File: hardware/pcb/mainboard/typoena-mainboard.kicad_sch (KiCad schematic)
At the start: 30 parts, among them J1 DESPI-C579, J2 UART-PROG, J3 MT3608-IN, J4 MT3608-OUT-5V, J5 BTN-JST-XH, J6 HARNESS-PCB2, Q1 AO3401A, Q2 AO3401A, Q3 2N7002, SW1 RESET, SW2 BOOT, U1 ESP32-S3-WROOM-1-N16R8, U2 AMS1117-3.3

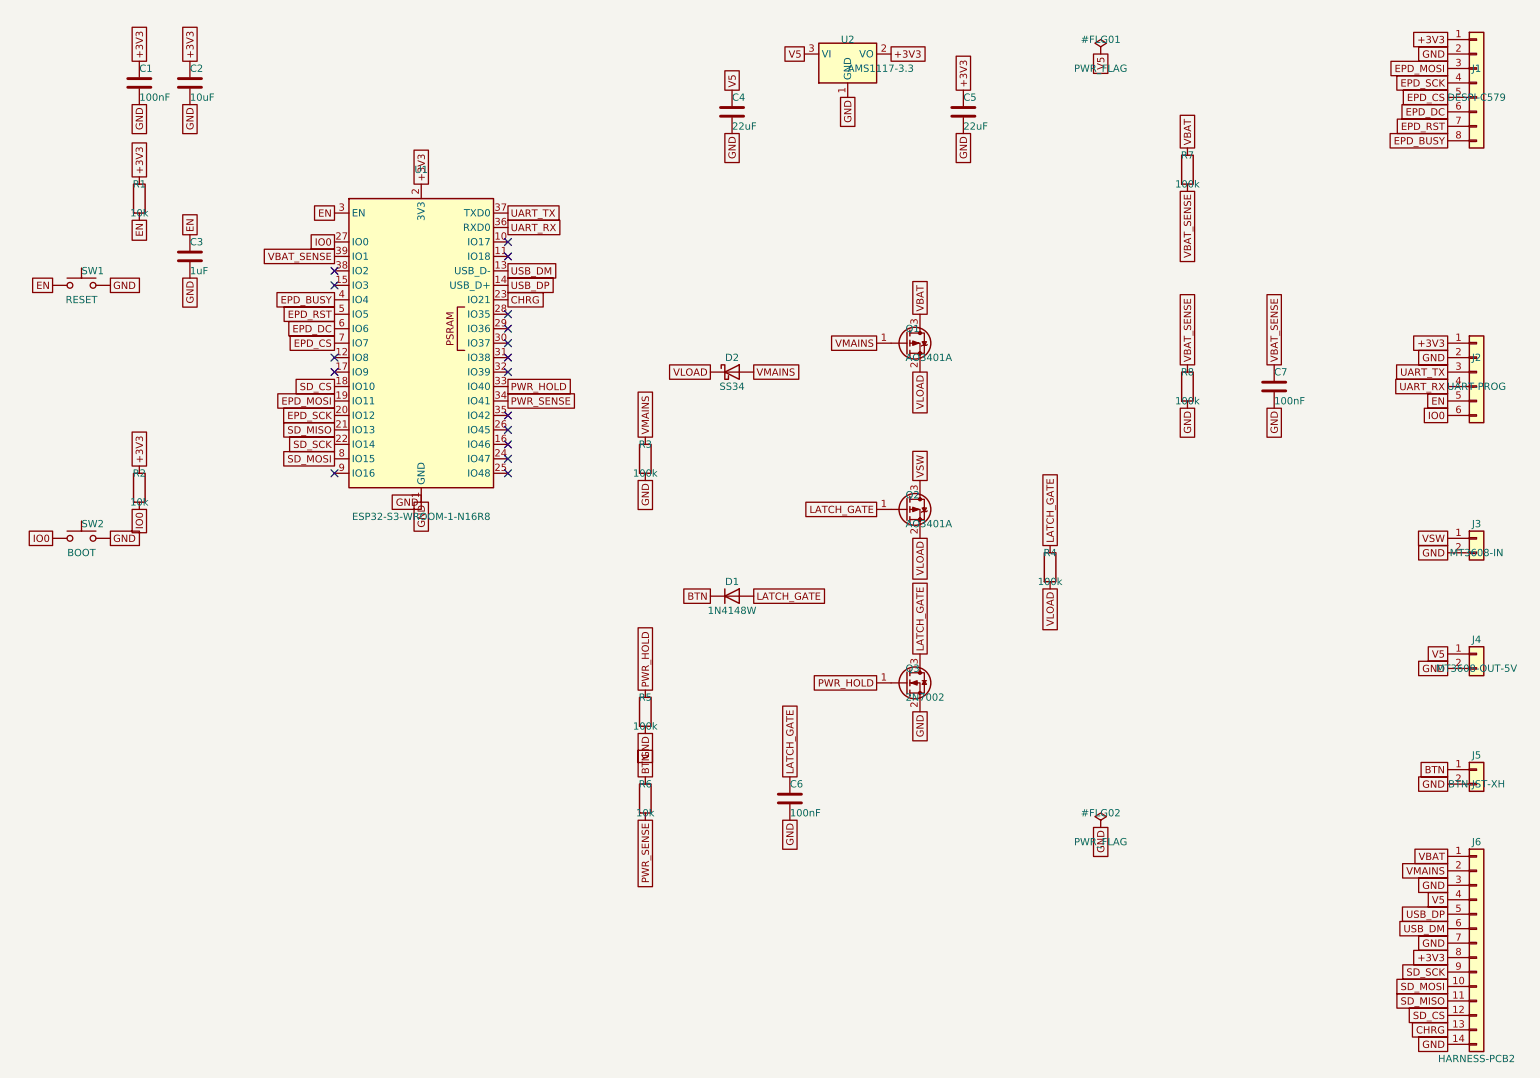
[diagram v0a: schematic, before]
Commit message: refactor(pcb): collapse to a single mainboard project
The two-perfboard design around the DevKitC-1 is gone; mainboard-v2 takes
the mainboard/ name and the -v2 suffix leaves every filename. The KiCad
project name is rewritten inside the instance blocks of all five sheets
too, otherwise KiCad drops the footprint assignments on open. ERC and DRC
still report 0 violations.

Add a Ground net class, split off Power, so GND carries its own via size
for the stitching and shows up in its own colour while routing. Its 0.2 mm
clearance is the neutral value: clearance resolves to the larger of the two
classes, so it never widens a gap on its own.

Drop the GPIO table from hardware/pcb/README.md rather than move it — the
netlist disagrees with it. PWR_HOLD no longer exists, PWR_SENSE is IO21 and
not IO41, and battery level comes from the BQ25896 over I2C instead of an
ADC. mainboard/README.md carries the pin plan that ships. wiring.md keeps
its bench-build pinout but stops attributing it to the deleted board.

hardware/bom.md, hardware/wiring.md and hardware/case/ still describe the
bench build, tracked as a TODO in the mainboard README.

Co-Authored-By: Claude Opus 5 <noreply@anthropic.com>
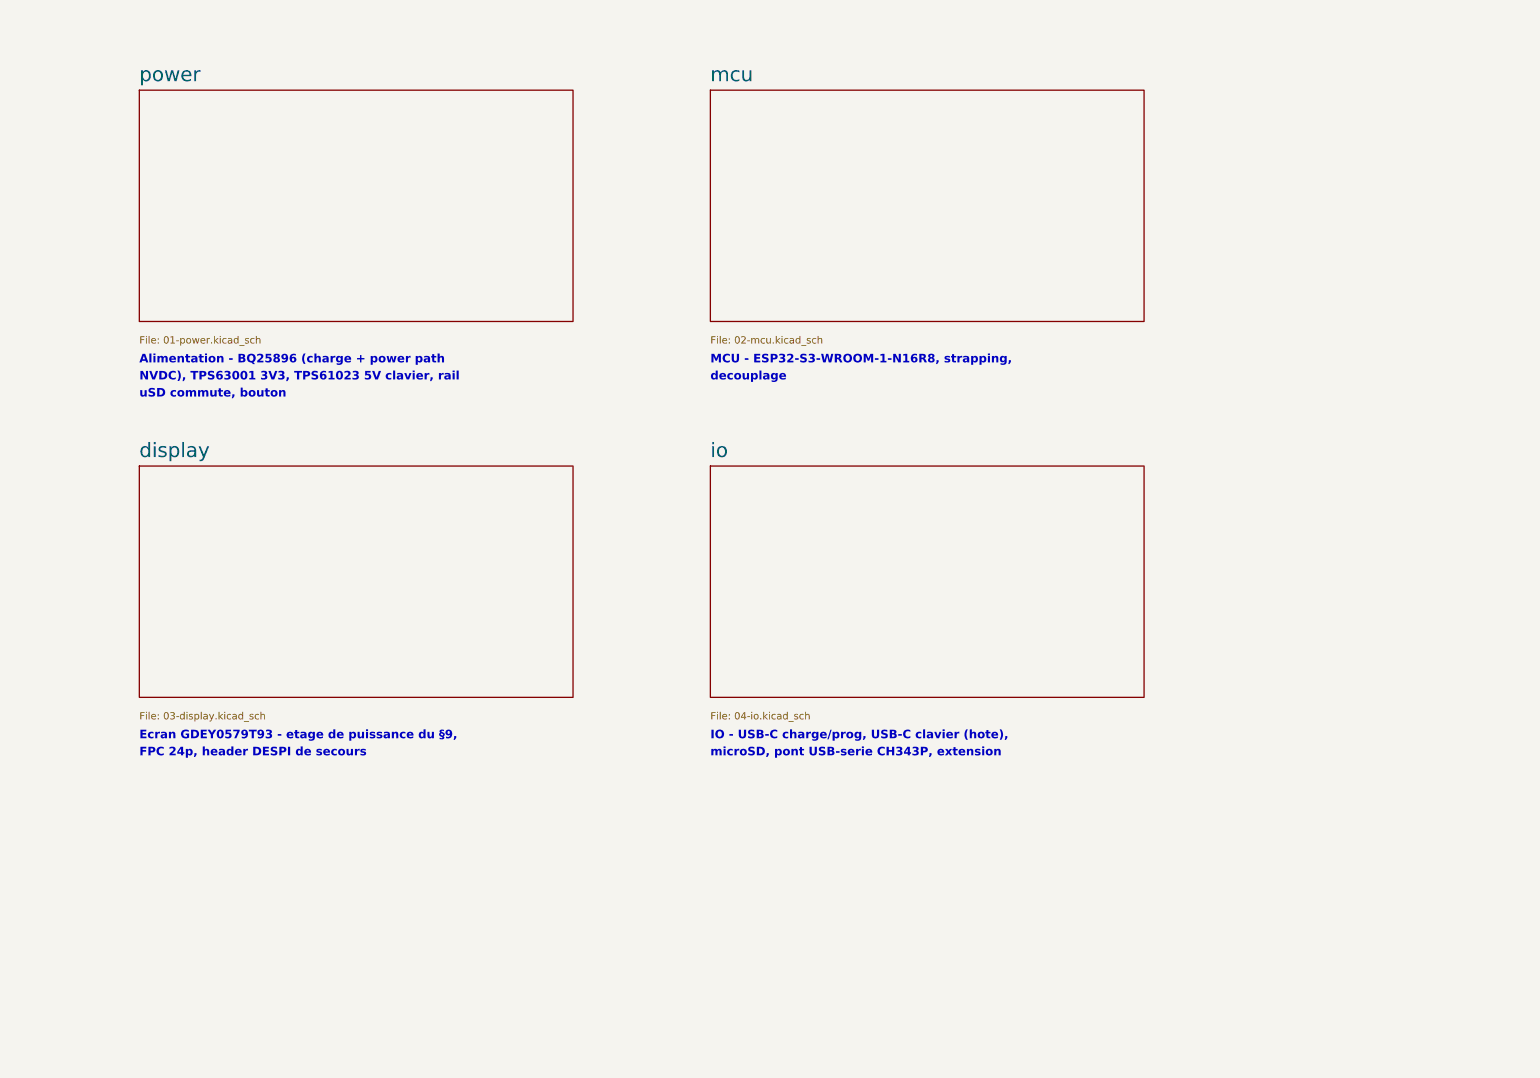
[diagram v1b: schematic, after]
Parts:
- removed C1, C6, C7: 100nF, Capacitor_SMD:C_0805_2012Metric, symbol Device:C
- removed C2: 10uF, Capacitor_SMD:C_0805_2012Metric, symbol Device:C
- removed C3: 1uF, Capacitor_SMD:C_0805_2012Metric, symbol Device:C
- removed C4, C5: 22uF, Capacitor_SMD:C_0805_2012Metric, symbol Device:C
- removed D1: 1N4148W, Diode_SMD:D_SOD-123, symbol Diode:1N4148W
- removed D2: SS34, Diode_SMD:D_SMA, symbol Diode:SS34
- removed J1: DESPI-C579, Connector_PinHeader_2.54mm:PinHeader_1x08_P2.54mm_Vertical, symbol Connector_Generic:Conn_01x08
- removed J2: UART-PROG, Connector_PinHeader_2.54mm:PinHeader_1x06_P2.54mm_Vertical, symbol Connector_Generic:Conn_01x06
- removed J3: MT3608-IN, Connector_PinHeader_2.54mm:PinHeader_1x02_P2.54mm_Vertical, symbol Connector_Generic:Conn_01x02
- removed J4: MT3608-OUT-5V, Connector_PinHeader_2.54mm:PinHeader_1x02_P2.54mm_Vertical, symbol Connector_Generic:Conn_01x02
- removed J5: BTN-JST-XH, Connector_PinHeader_2.54mm:PinHeader_1x02_P2.54mm_Vertical, symbol Connector_Generic:Conn_01x02
- removed J6: HARNESS-PCB2, Connector_PinHeader_2.54mm:PinHeader_1x14_P2.54mm_Vertical, symbol Connector_Generic:Conn_01x14
- removed Q1, Q2: AO3401A, Package_TO_SOT_SMD:SOT-23, symbol Transistor_FET:AO3401A
- removed Q3: 2N7002, Package_TO_SOT_SMD:SOT-23, symbol Transistor_FET:2N7002
- removed R1, R2, R6: 10k, Resistor_SMD:R_0805_2012Metric, symbol Device:R
- removed R3, R4, R5, R7, R8: 100k, Resistor_SMD:R_0805_2012Metric, symbol Device:R
- removed SW1: RESET, Button_Switch_SMD:SW_SPST_B3U-1000P, symbol Switch:SW_Push
- removed SW2: BOOT, Button_Switch_SMD:SW_SPST_B3U-1000P, symbol Switch:SW_Push
- removed U1: ESP32-S3-WROOM-1-N16R8, RF_Module:ESP32-S3-WROOM-1, symbol RF_Module:ESP32-S3-WROOM-1
- removed U2: AMS1117-3.3, Package_TO_SOT_SMD:SOT-223-3_TabPin2, symbol Regulator_Linear:AMS1117-3.3
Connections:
- no-connect marks 17 -> 0
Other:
- added sheet display (03-display.kicad_sch)
- added sheet io (04-io.kicad_sch)
- added sheet mcu (02-mcu.kicad_sch)
- added sheet power (01-power.kicad_sch)
- note added: "Alimentation - BQ25896 (charge + power path"
- note added: "Ecran GDEY0579T93 - etage de puissance du §9,"
- note added: "FPC 24p, header DESPI de secours"
- note added: "IO - USB-C charge/prog, USB-C clavier (hote),"
- note added: "MCU - ESP32-S3-WROOM-1-N16R8, strapping,"
- note added: "NVDC), TPS63001 3V3, TPS61023 5V clavier, rail"
- note added: "decouplage"
- note added: "microSD, pont USB-serie CH343P, extension"
- note added: "uSD commute, bouton"
- title: Typoena mainboard (PCB 1) -> Typoena mainboard

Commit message: feat(pcb): route the mainboard and add the design checker
801 segments, 110 vias, five filled zones, no unconnected net. Board is
94x45 mm with four #6-32 corner holes; D2 dropped and GPIO 48 exposed on
J10; J4 mechanical pin tied to GND.

tools/check_pcb.py consolidates the checks that were improvised until now:
switching-node discipline, hot loops, decoupling, via-in-pad, fine-pitch
escapes, current capacity, schematic/PCB cross-checks.

Co-Authored-By: Claude Opus 5 <noreply@anthropic.com>
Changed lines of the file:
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@@
 (kicad_sch
-	(version 20250114)
-	(generator "typoena")
+	(version 20260306)
+	(generator "eeschema")
 	(generator_version "10.0")
 	(paper "A4")
@@
 		(comment 2 "Connectivite inter-feuilles par etiquettes globales")
 	)
+	(text "uSD commute, bouton"
+		(exclude_from_sim no)
+		(at 30.48 99.98 0)
+		(effects
+			(font
+				(size 1.5 1.5)
+				(bold yes)
+			)
+			(justify left bottom)
+		)
+	)
+	(text "NVDC), TPS63001 3V3, TPS61023 5V clavier, rail"
+		(exclude_from_sim no)
+		(at 30.48 96.98 0)
+		(effects
+			(font
+				(size 1.5 1.5)
+				(bold yes)
+			)
+			(justify left bottom)
+		)
+	)
+	(text "Ecran GDEY0579T93 - etage de puissance du §9,"
+		(exclude_from_sim no)
+		(at 30.48 160.02 0)
+		(effects
+			(font
+				(size 1.5 1.5)
+				(bold yes)
+			)
+			(justify left bottom)
+		)
+	)
+	(text "IO - USB-C charge/prog, USB-C clavier (hote),"
+		(exclude_from_sim no)
+		(at 130.81 160.02 0)
+		(effects
+			(font
+				(size 1.5 1.5)
+				(bold yes)
+			)
+			(justify left bottom)
+		)
+	)
+	(text "decouplage"
+		(exclude_from_sim no)
+		(at 130.81 96.98 0)
+		(effects
+			(font
+				(size 1.5 1.5)
+				(bold yes)
+			)
+			(justify left bottom)
+		)
+	)
+	(text "microSD, pont USB-serie CH343P, extension"
+		(exclude_from_sim no)
+		(at 130.81 163.02 0)
+		(effects
+			(font
+				(size 1.5 1.5)
+				(bold yes)
+			)
+			(justify left bottom)
+		)
+	)
+	(text "FPC 24p, header DESPI de secours"
+		(exclude_from_sim no)
+		(at 30.48 163.02 0)
+		(effects
+			(font
+				(size 1.5 1.5)
+				(bold yes)
+			)
+			(justify left bottom)
+		)
+	)
+	(text "Alimentation - BQ25896 (charge + power path"
+		(exclude_from_sim no)
+		(at 30.48 93.98 0)
+		(effects
+			(font
+				(size 1.5 1.5)
+				(bold yes)
+			)
+			(justify left bottom)
+		)
+	)
+	(text "MCU - ESP32-S3-WROOM-1-N16R8, strapping,"
+		(exclude_from_sim no)
+		(at 130.81 93.98 0)
+		(effects
+			(font
+				(size 1.5 1.5)
+				(bold yes)
+			)
+			(justify left bottom)
+		)
+	)
 	(sheet
 		(at 30.48 45.72)
 		(size 76.2 40.64)
-		(fields_autoplaced yes)
-		(stroke
-			(width 0.1524)
-			(type solid)
-		)
-		(fill
-			(color 0 0 0 0.0000)
+		(exclude_from_sim no)
+		(in_bom yes)
+		(on_board yes)
+		(dnp no)
+		(fields_autoplaced yes)
+		(stroke
+			(width 0.1524)
+			(type solid)
+		)
+		(fill
+			(color 0 0 0 0)
 		)
 		(property "Sheetname" "power"
-			(at 30.48 44.449999999999996 0)
+			(at 30.48 44.45 0)
+			(show_name no)
+			(do_not_autoplace no)
 			(effects
 				(font
@@
 		(property "Sheetfile" "01-power.kicad_sch"
 			(at 30.48 88.9 0)
+			(show_name no)
+			(do_not_autoplace no)
 			(effects
 				(font
@@
 		)
 	)
-	(text "Alimentation - BQ25896 (charge + power path"
-		(exclude_from_sim no)
-		(at 30.48 93.98 0)
-		(effects
-			(font
-				(size 1.5 1.5)
-				(bold yes)
-			)
-			(justify left bottom)
-		)
-	)
-	(text "NVDC), TPS63001 3V3, TPS61023 5V clavier, rail"
-		(exclude_from_sim no)
-		(at 30.48 96.98 0)
-		(effects
-			(font
-				(size 1.5 1.5)
-				(bold yes)
-			)
-			(justify left bottom)
-		)
-	)
-	(text "uSD commute, bouton"
-		(exclude_from_sim no)
-		(at 30.48 99.98 0)
-		(effects
-			(font
-				(size 1.5 1.5)
-				(bold yes)
-			)
-			(justify left bottom)
-		)
-	)
 	(sheet
 		(at 130.81 45.72)
 		(size 76.2 40.64)
-		(fields_autoplaced yes)
-		(stroke
-			(width 0.1524)
-			(type solid)
-		)
-		(fill
-			(color 0 0 0 0.0000)
+		(exclude_from_sim no)
+		(in_bom yes)
+		(on_board yes)
+		(dnp no)
+		(fields_autoplaced yes)
+		(stroke
+			(width 0.1524)
+			(type solid)
+		)
+		(fill
+			(color 0 0 0 0)
 		)
 		(property "Sheetname" "mcu"
-			(at 130.81 44.449999999999996 0)
+			(at 130.81 44.45 0)
+			(show_name no)
+			(do_not_autoplace no)
 			(effects
 				(font
@@
 		(property "Sheetfile" "02-mcu.kicad_sch"
 			(at 130.81 88.9 0)
+			(show_name no)
+			(do_not_autoplace no)
 			(effects
 				(font
@@
 		)
 	)
-	(text "MCU - ESP32-S3-WROOM-1-N16R8, strapping,"
-		(exclude_from_sim no)
-		(at 130.81 93.98 0)
-		(effects
-			(font
-				(size 1.5 1.5)
-				(bold yes)
-			)
-			(justify left bottom)
-		)
-	)
-	(text "decouplage"
-		(exclude_from_sim no)
-		(at 130.81 96.98 0)
-		(effects
-			(font
-				(size 1.5 1.5)
-				(bold yes)
-			)
-			(justify left bottom)
-		)
-	)
 	(sheet
 		(at 30.48 111.76)
 		(size 76.2 40.64)
-		(fields_autoplaced yes)
-		(stroke
-			(width 0.1524)
-			(type solid)
-		)
-		(fill
-			(color 0 0 0 0.0000)
+		(exclude_from_sim no)
+		(in_bom yes)
+		(on_board yes)
+		(dnp no)
+		(fields_autoplaced yes)
+		(stroke
+			(width 0.1524)
+			(type solid)
+		)
+		(fill
+			(color 0 0 0 0)
 		)
 		(property "Sheetname" "display"
-			(at 30.48 110.49000000000001 0)
+			(at 30.48 110.49 0)
+			(show_name no)
+			(do_not_autoplace no)
 			(effects
 				(font
@@
 		(property "Sheetfile" "03-display.kicad_sch"
 			(at 30.48 154.94 0)
+			(show_name no)
+			(do_not_autoplace no)
 			(effects
 				(font
@@
 		)
 	)
-	(text "Ecran GDEY0579T93 - etage de puissance du §9,"
-		(exclude_from_sim no)
-		(at 30.48 160.02 0)
-		(effects
-			(font
-				(size 1.5 1.5)
-				(bold yes)
-			)
-			(justify left bottom)
-		)
-	)
-	(text "FPC 24p, header DESPI de secours"
-		(exclude_from_sim no)
-		(at 30.48 163.02 0)
-		(effects
-			(font
-				(size 1.5 1.5)
-				(bold yes)
-			)
-			(justify left bottom)
-		)
-	)
 	(sheet
 		(at 130.81 111.76)
 		(size 76.2 40.64)
-		(fields_autoplaced yes)
-		(stroke
-			(width 0.1524)
-			(type solid)
-		)
-		(fill
-			(color 0 0 0 0.0000)
+		(exclude_from_sim no)
+		(in_bom yes)
+		(on_board yes)
+		(dnp no)
+		(fields_autoplaced yes)
+		(stroke
+			(width 0.1524)
+			(type solid)
+		)
+		(fill
+			(color 0 0 0 0)
 		)
 		(property "Sheetname" "io"
-			(at 130.81 110.49000000000001 0)
+			(at 130.81 110.49 0)
+			(show_name no)
+			(do_not_autoplace no)
 			(effects
 				(font
@@
 		(property "Sheetfile" "04-io.kicad_sch"
 			(at 130.81 154.94 0)
+			(show_name no)
+			(do_not_autoplace no)
 			(effects
 				(font
@@
 		)
 	)
-	(text "IO - USB-C charge/prog, USB-C clavier (hote),"
-		(exclude_from_sim no)
-		(at 130.81 160.02 0)
-		(effects
-			(font
-				(size 1.5 1.5)
-				(bold yes)
-			)
-			(justify left bottom)
-		)
-	)
-	(text "microSD, pont USB-serie CH343P, extension"
-		(exclude_from_sim no)
-		(at 130.81 163.02 0)
-		(effects
-			(font
-				(size 1.5 1.5)
-				(bold yes)
-			)
-			(justify left bottom)
-		)
-	)
